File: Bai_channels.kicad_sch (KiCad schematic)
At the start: 24 parts, among them U1 ATmega328-P, U3 LM7805_TO220

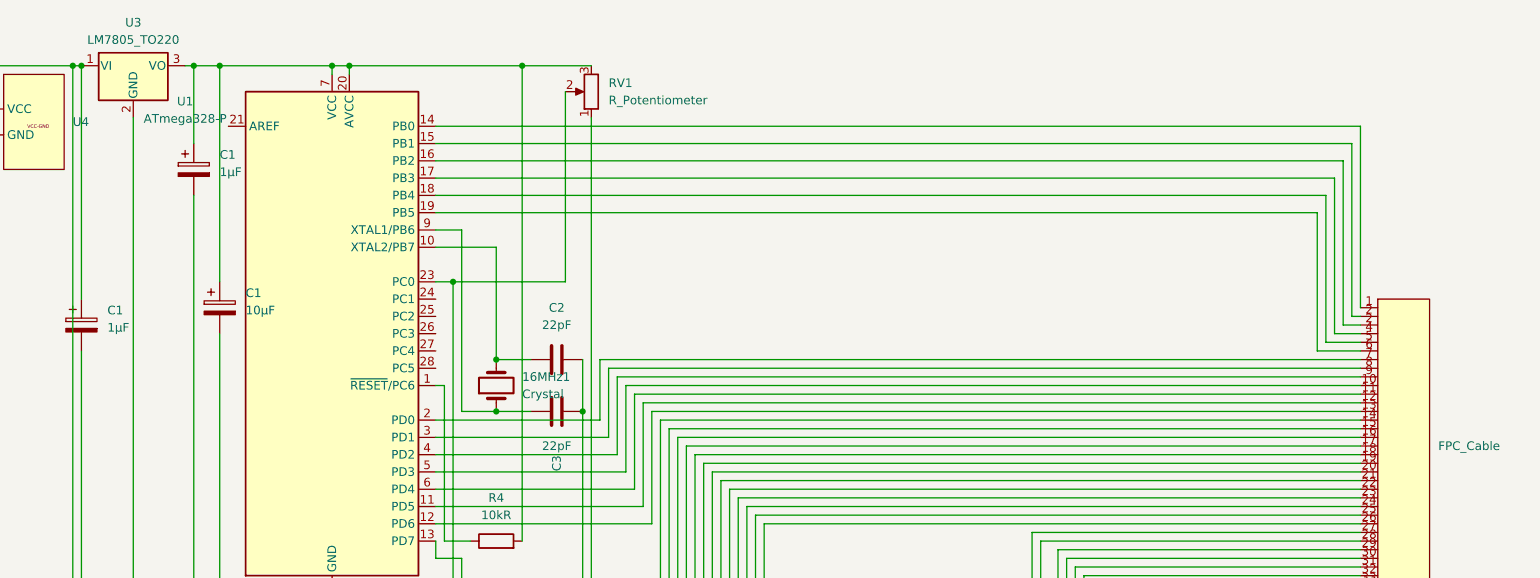
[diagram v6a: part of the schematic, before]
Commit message: custom cable footprint
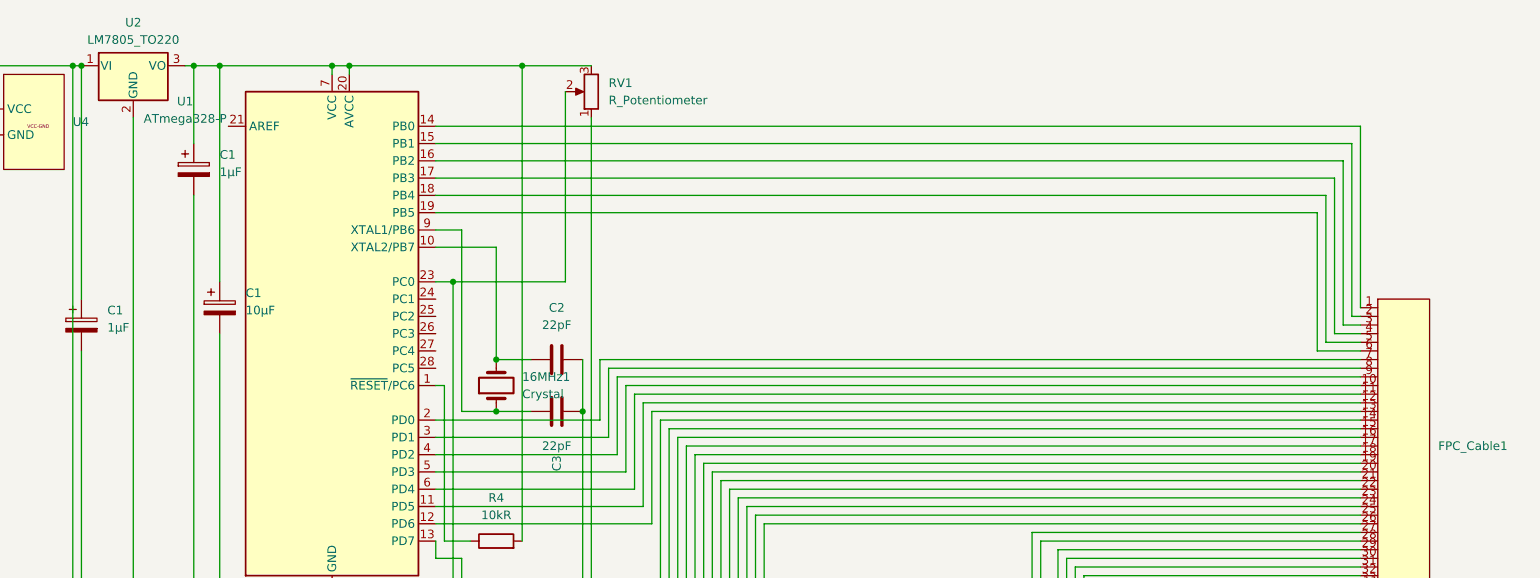
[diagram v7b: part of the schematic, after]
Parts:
- removed FPC_Cable: ~, symbol Custom_Symbol_Lib:FCP_Cable
- added FPC_Cable1: ~, custom:FPC_Cable, symbol Custom_Symbol_Lib:FCP_Cable
- renumbered U3 to U2
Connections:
- net at C1.2, C1.2, C1.2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: now also FPC_Cable1.33 (GND)
- net at U1.14 (PB0): now also FPC_Cable1.1
- net at U1.5 (PD3): now also FPC_Cable1.10
- net at U1.6 (PD4): now also FPC_Cable1.11
- net at U1.11 (PD5): now also FPC_Cable1.12
- net at U1.12 (PD6): now also FPC_Cable1.13
- net at U1.14 (PB0): now also FPC_Cable1.14
- net at U1.15 (PB1): now also FPC_Cable1.15
- net at U1.16 (PB2): now also FPC_Cable1.16
- net at U1.17 (PB3): now also FPC_Cable1.17
- net at U1.18 (PB4): now also FPC_Cable1.18
- net at U1.19 (PB5): now also FPC_Cable1.19
- net at U1.15 (PB1): now also FPC_Cable1.2
- net at U1.16 (PB2): now also FPC_Cable1.3
- net at U1.2 (PD0): now also FPC_Cable1.20
- net at U1.3 (PD1): now also FPC_Cable1.21
- net at U1.4 (PD2): now also FPC_Cable1.22
- net at U1.5 (PD3): now also FPC_Cable1.23
- net at U1.6 (PD4): now also FPC_Cable1.24
- net at U1.11 (PD5): now also FPC_Cable1.25
- net at U1.12 (PD6): now also FPC_Cable1.26
- net at U1.14 (PB0): now also FPC_Cable1.27
- net at U1.15 (PB1): now also FPC_Cable1.28
- net at U1.16 (PB2): now also FPC_Cable1.29
- net at U1.17 (PB3): now also FPC_Cable1.30
- net at U1.18 (PB4): now also FPC_Cable1.31
- net at U1.19 (PB5): now also FPC_Cable1.32
- net at U1.17 (PB3): now also FPC_Cable1.4
- net at U1.18 (PB4): now also FPC_Cable1.5
- net at U1.19 (PB5): now also FPC_Cable1.6
- net at U1.2 (PD0): now also FPC_Cable1.7
- net at U1.3 (PD1): now also FPC_Cable1.8
- net at U1.4 (PD2): now also FPC_Cable1.9

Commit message: Official FPC
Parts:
- removed FPC_Cable1: ~, custom:FPC_Cable, symbol Custom_Symbol_Lib:FCP_Cable
- added J2: 5019514000, custom:CON_5019514000, symbol Custom_Symbol_Lib:5019514000
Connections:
- net at C1.2, C1.2, C1.2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: now also J2.33
- net at U1.14 (PB0): now also J2.1
- net at U1.5 (PD3): now also J2.10
- net at U1.6 (PD4): now also J2.11
- net at U1.11 (PD5): now also J2.12
- net at U1.12 (PD6): now also J2.13
- net at U1.14 (PB0): now also J2.14
- net at U1.15 (PB1): now also J2.15
- net at U1.16 (PB2): now also J2.16
- net at U1.17 (PB3): now also J2.17
- net at U1.18 (PB4): now also J2.18
- net at U1.19 (PB5): now also J2.19
- net at U1.15 (PB1): now also J2.2
- net at U1.2 (PD0): now also J2.20
- net at U1.3 (PD1): now also J2.21
- net at U1.4 (PD2): now also J2.22
- net at U1.5 (PD3): now also J2.23
- net at U1.6 (PD4): now also J2.24
- net at U1.11 (PD5): now also J2.25
- net at U1.12 (PD6): now also J2.26
- net at U1.14 (PB0): now also J2.27
- net at U1.15 (PB1): now also J2.28
- net at U1.16 (PB2): now also J2.29
- net at U1.16 (PB2): now also J2.3
- net at U1.17 (PB3): now also J2.30
- net at U1.18 (PB4): now also J2.31
- net at U1.19 (PB5): now also J2.32
- net at U1.17 (PB3): now also J2.4
- net at U1.18 (PB4): now also J2.5
- net at U1.19 (PB5): now also J2.6
- net at U1.2 (PD0): now also J2.7
- net at U1.3 (PD1): now also J2.8
- net at U1.4 (PD2): now also J2.9
